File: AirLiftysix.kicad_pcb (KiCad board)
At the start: 2 copper layers, 0 parts

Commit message: started on PCB
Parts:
- added C1: 10u, Capacitor_SMD:C_0201_0603Metric_Pad0.64x0.40mm_HandSolder, F.Cu at (229.0, 89.6)
- added C2: 10u, Capacitor_SMD:C_0201_0603Metric_Pad0.64x0.40mm_HandSolder, F.Cu at (229.0, 91.3)
- added C3: 10u, Capacitor_SMD:C_0201_0603Metric_Pad0.64x0.40mm_HandSolder, F.Cu at (229.0, 93.1)
- added C4: 0.1u, Capacitor_SMD:C_0201_0603Metric_Pad0.64x0.40mm_HandSolder, F.Cu at (229.0, 94.8)
- added D1: LED, LED_SMD:LED_0603_1608Metric_Pad1.05x0.95mm_HandSolder, F.Cu at (229.8, 100.5)
- added D2: LED, LED_SMD:LED_0603_1608Metric_Pad1.05x0.95mm_HandSolder, F.Cu at (229.8, 103.1)
- added D3: LED, LED_SMD:LED_0603_1608Metric_Pad1.05x0.95mm_HandSolder, F.Cu at (229.8, 105.7)
- added J1: Conn_01x12_Socket, Connector_PinHeader_2.54mm:PinHeader_1x12_P2.54mm_Vertical, F.Cu at (182.9, 124.5)
- added Q1: BSS138, Package_TO_SOT_SMD:SOT-23, F.Cu at (209.9, 119.0)
- added R1: 1K, Resistor_SMD:R_0201_0603Metric_Pad0.64x0.40mm_HandSolder, F.Cu at (229.0, 96.6)
- added R2: 1K, Resistor_SMD:R_0201_0603Metric_Pad0.64x0.40mm_HandSolder, F.Cu at (229.0, 98.3)
- added R3: 1K, Resistor_SMD:R_0201_0603Metric_Pad0.64x0.40mm_HandSolder, F.Cu at (231.8, 89.6)
- added R4: R_US, Resistor_SMD:R_0201_0603Metric_Pad0.64x0.40mm_HandSolder, F.Cu at (231.8, 91.3)
- added R5: R_US, Resistor_SMD:R_0201_0603Metric_Pad0.64x0.40mm_HandSolder, F.Cu at (231.8, 93.1)
- added R6: 10K, Resistor_SMD:R_0201_0603Metric_Pad0.64x0.40mm_HandSolder, F.Cu at (231.8, 94.8)
- added R7: 10K, Resistor_SMD:R_0201_0603Metric_Pad0.64x0.40mm_HandSolder, F.Cu at (231.8, 96.6)
- added U1: AP2112K-3.3, Package_TO_SOT_SMD:SOT-23-5, F.Cu at (209.6, 99.1)
- added U4: ESP32-WROOM-32UE-R2, RF_Module:ESP32-WROOM-32UE, F.Cu at (196.4, 109.0)
- added U5: 74HC4050D, Package_SO:SOIC-16_3.9x9.9mm_P1.27mm, F.Cu at (212.2, 109.9)
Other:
- board outline added: 31.8 x 33 mm

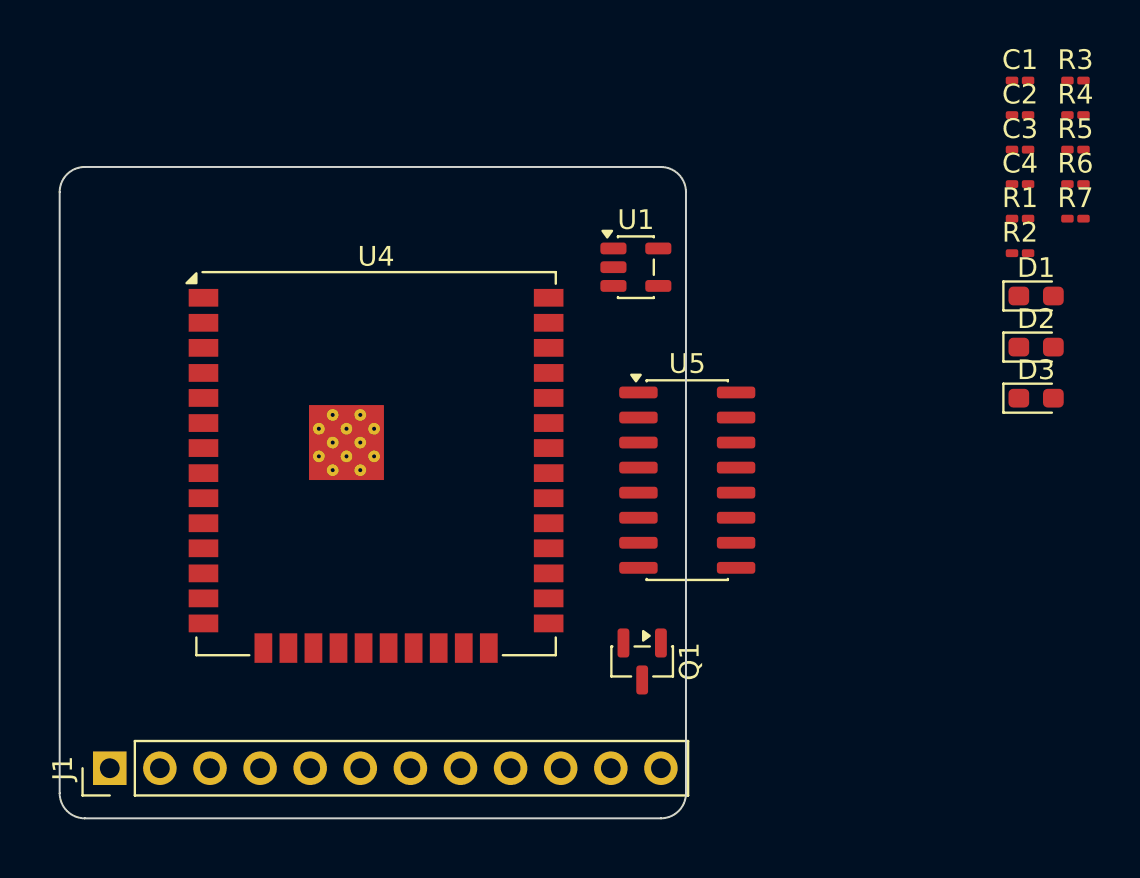
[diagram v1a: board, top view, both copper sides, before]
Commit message: includes antenna
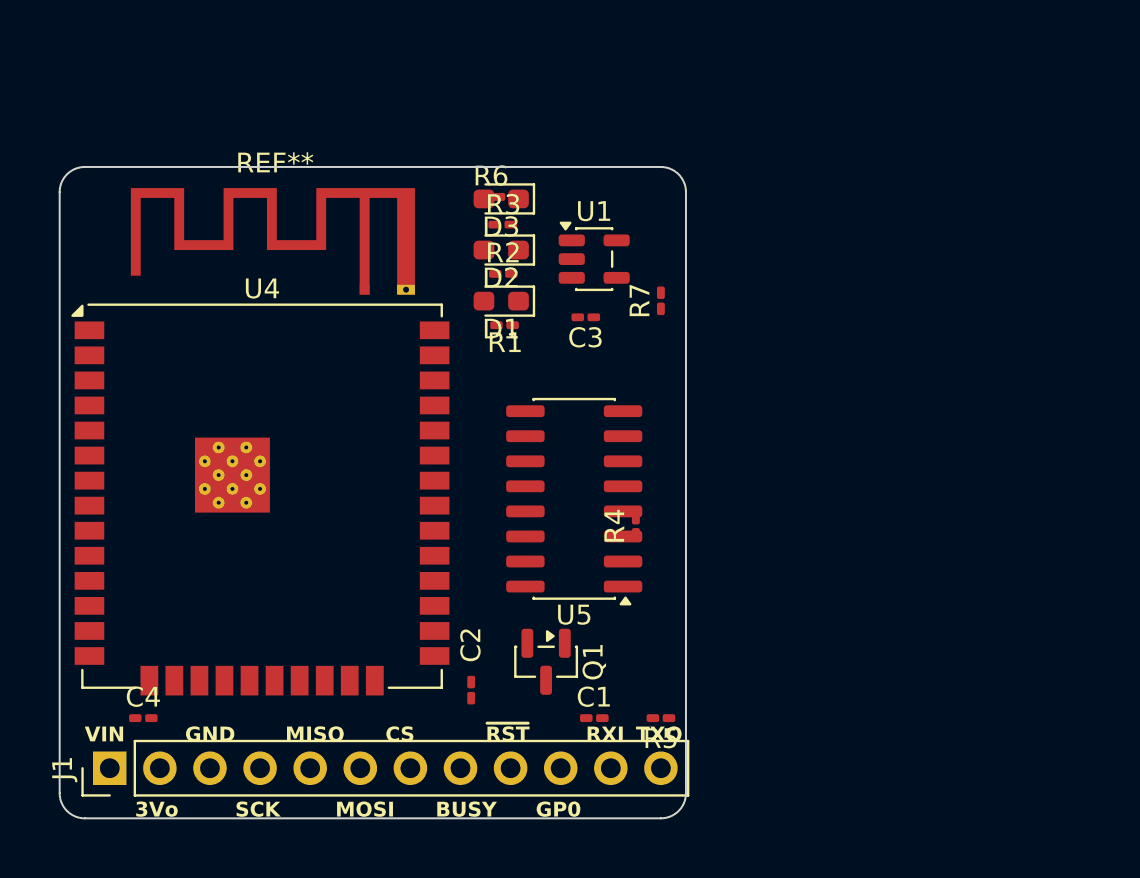
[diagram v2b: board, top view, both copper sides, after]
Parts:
- added REF**: Texas_SWRA117D_2.4GHz_Left, RF_Antenna:Texas_SWRA117D_2.4GHz_Left, F.Cu at (195.8, 100.2)
- moved C4 52.0 mm to (184.6, 121.9)
- moved C2 40.3 mm to (201.2, 120.5), turned to 90 degrees
- moved C1 38.9 mm to (207.4, 121.9)
- moved R5 35.7 mm to (210.8, 121.9), turned to 180 degrees
- moved R4 30.5 mm to (209.6, 112.2), turned to 90 degrees
- moved R3 29.9 mm to (202.8, 96.9)
- moved R6 29.6 mm to (202.2, 95.5)
- moved D3 28.9 mm to (202.7, 95.6), turned to 180 degrees
- moved D2 27.6 mm to (202.7, 98.2), turned to 180 degrees
- moved D1 27.1 mm to (202.7, 100.8), turned to 180 degrees
- moved R1 26.7 mm to (202.9, 102.0), turned to 180 degrees
- moved R2 26.2 mm to (202.8, 99.4)
- moved C3 23.6 mm to (207.0, 101.6), turned to 180 degrees
- moved R7 21.4 mm to (210.8, 100.8), turned to 90 degrees
- moved U4 6.01 mm to (190.6, 110.7)
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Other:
- board text added: "3Vo"
- board text added: "BUSY"
- board text added: "CS"
- board text added: "GND"
- board text added: "GP0"
- board text added: "MISO"
- board text added: "MOSI"
- board text added: "Notes: 1. See https://www.ti.com/lit/an/swru120d/swru120d.pdf"
- board text added: "RXI"
- board text added: "SCK"
- board text added: "TXO"
- board text added: "VIN"
- board text added: "~{RST}"

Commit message: antenna, new floorplan
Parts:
- removed REF**: Texas_SWRA117D_2.4GHz_Left, RF_Antenna:Texas_SWRA117D_2.4GHz_Left
- added AE1: Antenna, RF_Antenna:Texas_SWRA117D_2.4GHz_Left, F.Cu at (196.1, 100.3)
- moved D3 31.0 mm to (181.4, 118.1), turned to -90 degrees
- moved R3 28.0 mm to (181.4, 114.9), turned to 90 degrees
- moved D1 24.0 mm to (181.5, 112.0), turned to -90 degrees
- moved D2 22.7 mm to (181.5, 106.2), turned to -90 degrees
- moved R1 22.7 mm to (181.4, 109.2), turned to 90 degrees
- moved R2 21.8 mm to (181.4, 103.3), turned to 90 degrees
- moved R6 11.1 mm to (209.8, 103.6)
- moved U4 1.70 mm to (192.3, 110.6)
- moved U5 0.40 mm to (206.8, 110.8)
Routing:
- net /GREEN: track 0.00 -> 7.92 mm
- net /BLUE: track 0.00 -> 4.32 mm
- net /RED: track 0.00 -> 3.06 mm
- added copper zone on B.Cu, net GND
- added copper zone on F.Cu, net GND

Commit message: Added notes to PCB
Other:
- board text added: "Notes: 1. See https://www.ti.com/lit/an/swru120d/swru120d.pdf Decisions Made o Used KiCAD's antenna, added second pin. This is a flying wire. The issue is it avoids the 50 ohms exercise. o The 74HC4050 pinout is much bigger than the 74AHC4050. o Use the WiFi only module, not the WiFi + LoRa module - https://dwmzone.com/en/wireless-tag/1227-wtlrc262-sg-esp32-c2-sx1262-wifi-ble-lora-lorawan-module.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"
- board text removed: "Notes: 1. See https://www.ti.com/lit/an/swru120d/swru120d.pdf"
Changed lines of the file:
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@@
 		)
 	)
-	(gr_text "Notes:\n1.  See https://www.ti.com/lit/an/swru120d/swru120d.pdf\n"
-		(at 180.2 137.2 0)
+	(gr_text "Notes:\n1.  See https://www.ti.com/lit/an/swru120d/swru120d.pdf\n\nDecisions Made\no Used KiCAD's antenna, added second pin.  This is a flying wire.  The issue is it avoids the 50 ohms exercise.\no The 74HC4050 pinout is much bigger than the 74AHC4050.\no Use the WiFi only module, not the WiFi + LoRa module \n    - https://dwmzone.com/en/wireless-tag/1227-wtlrc262-sg-esp32-c2-sx1262-wifi-ble-lora-lorawan-module.html\no Use separate R's instead of the squarish quad R\no Same size as Adafruit's (larger will be easier to solder)\n"
+		(at 180.3 147.2 0)
 		(layer "User.1")
 		(effects
